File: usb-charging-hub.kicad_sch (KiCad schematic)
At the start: 3 parts

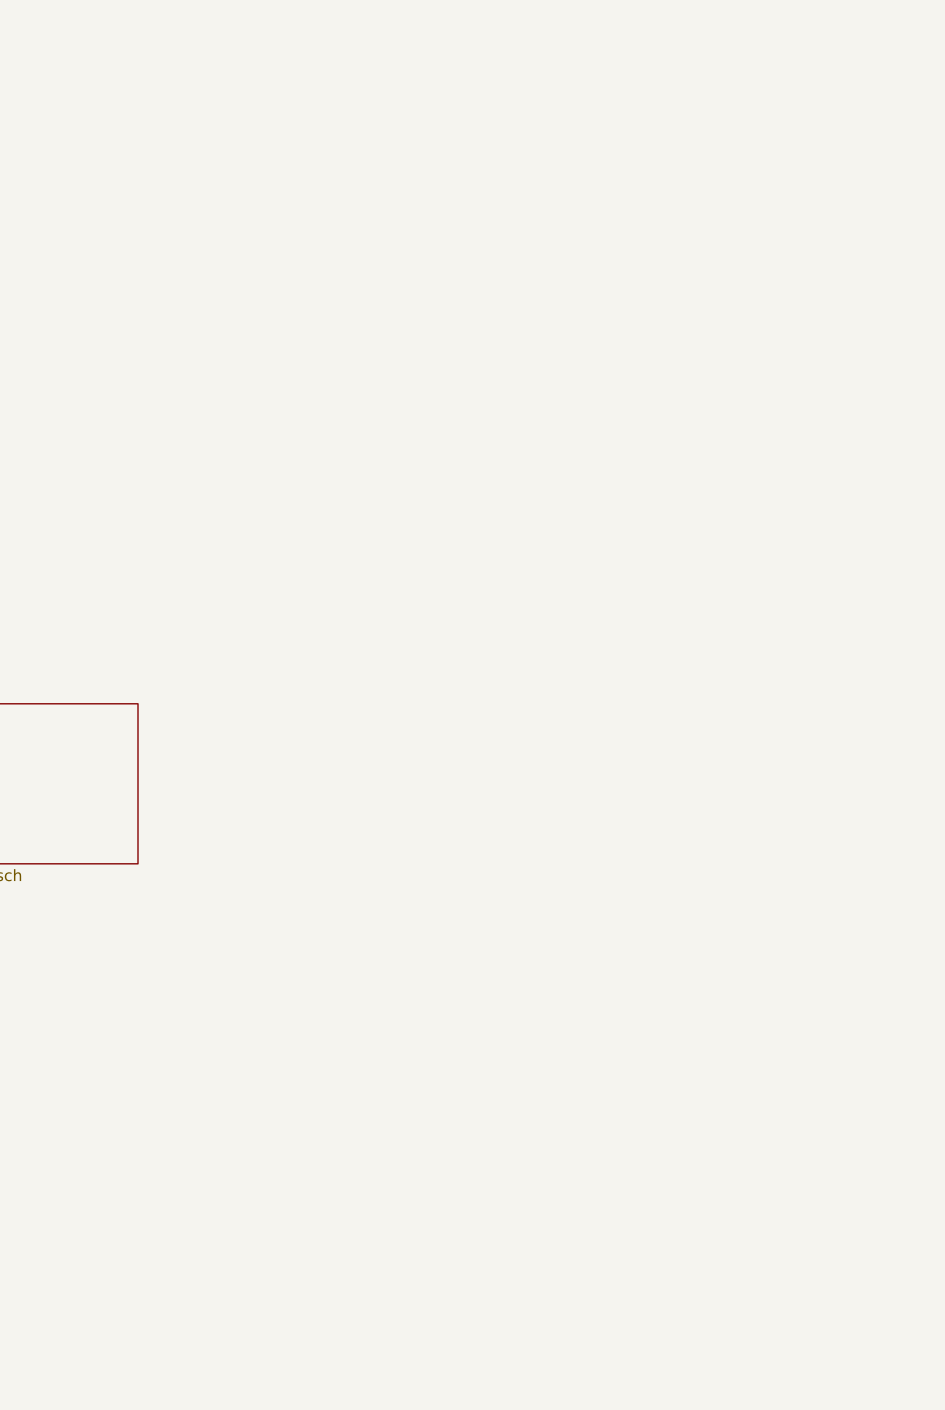
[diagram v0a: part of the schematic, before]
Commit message: fixed wrong wiring of 5V regulator for rp mcu + added all usb a ports
Signed-off-by: Toby Cm <toby@vsus.app>
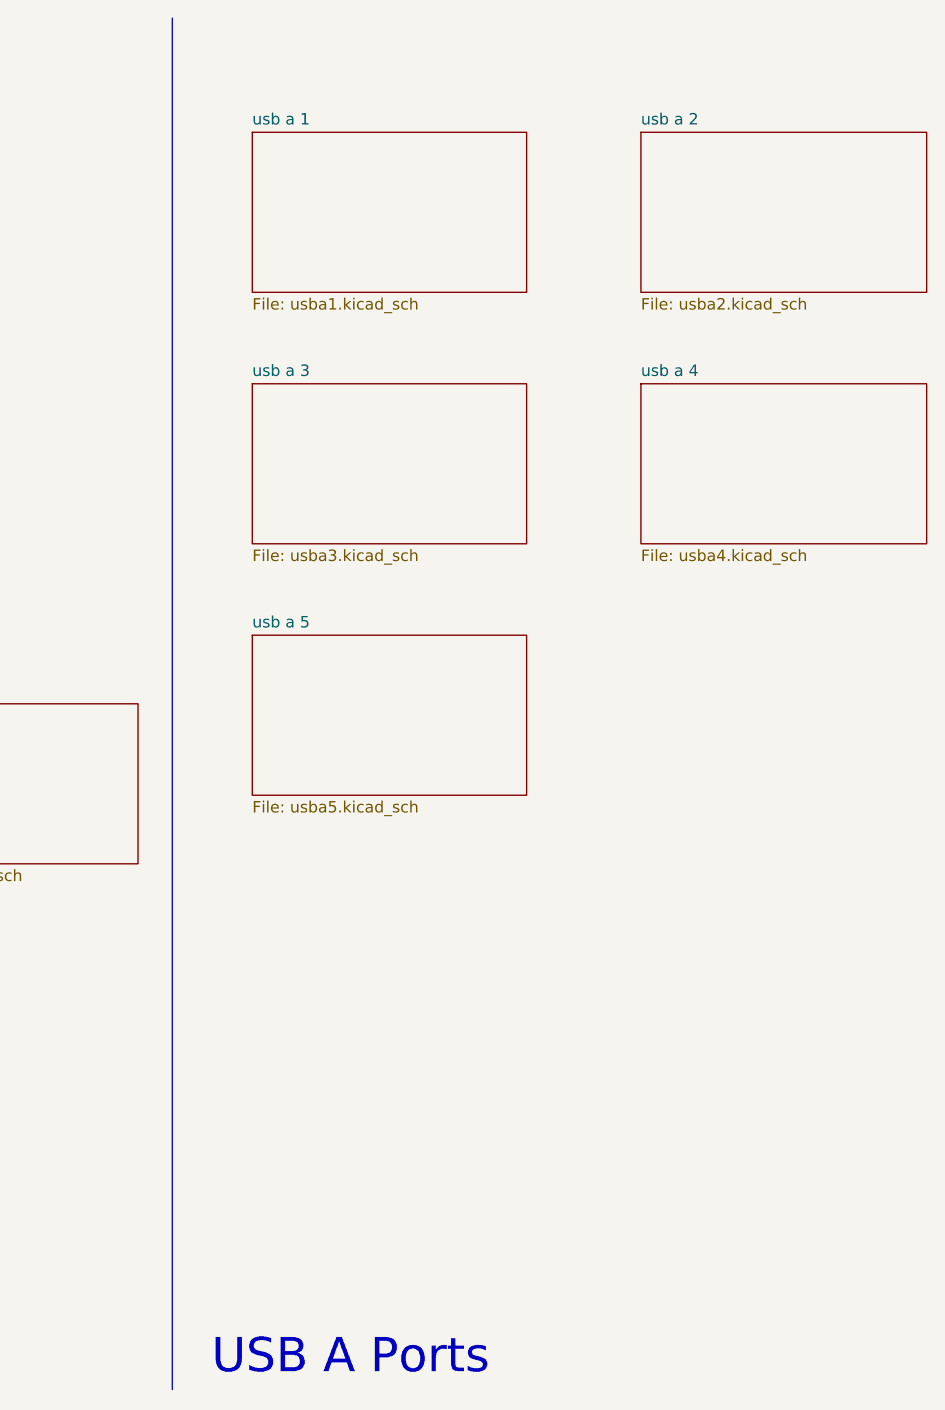
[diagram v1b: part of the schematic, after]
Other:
- added sheet usb a 1 (usba1.kicad_sch)
- added sheet usb a 2 (usba2.kicad_sch)
- added sheet usb a 3 (usba3.kicad_sch)
- added sheet usb a 4 (usba4.kicad_sch)
- added sheet usb a 5 (usba5.kicad_sch)
- note added: "USB A Ports"
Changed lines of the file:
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@@
 		(company "DaCloud")
+	)
+	(text "USB A Ports"
+		(exclude_from_sim no)
+		(at 211.582 161.544 0)
+		(effects
+			(font
+				(size 3.81 3.81)
+			)
+		)
 	)
 	(text "power led\n"
@@
 		)
 	)
+	(polyline
+		(pts
+			(xy 191.77 12.7) (xy 191.77 165.1)
+		)
+		(stroke
+			(width 0)
+			(type default)
+		)
+	)
 	(symbol
 		(lib_id "Jumper:SolderJumper_2_Bridged")
@@
 	)
 	(sheet
+		(at 243.84 25.4)
+		(size 31.75 17.78)
+		(exclude_from_sim no)
+		(in_bom yes)
+		(on_board yes)
+		(dnp no)
+		(fields_autoplaced yes)
+		(stroke
+			(width 0.1524)
+			(type solid)
+		)
+		(fill
+			(color 0 0 0 0.0000)
+		)
+		(property "Sheetname" "usb a 2"
+			(at 243.84 24.6884 0)
+			(effects
+				(font
+					(size 1.27 1.27)
+				)
+				(justify left bottom)
+			)
+		)
+		(property "Sheetfile" "usba2.kicad_sch"
+			(at 243.84 43.7646 0)
+			(effects
+				(font
+					(size 1.27 1.27)
+				)
+				(justify left top)
+			)
+		)
+		(instances
+			(project "usb-charging-hub"
+				(path "/04e54dfe-f06f-40ed-b860-573373578cb0"
+					(page "7")
+				)
+			)
+		)
+	)
+	(sheet
 		(at 22.86 88.9)
 		(size 30.48 17.78)
@@
 	)
 	(sheet
+		(at 200.66 81.28)
+		(size 30.48 17.78)
+		(exclude_from_sim no)
+		(in_bom yes)
+		(on_board yes)
+		(dnp no)
+		(fields_autoplaced yes)
+		(stroke
+			(width 0.1524)
+			(type solid)
+		)
+		(fill
+			(color 0 0 0 0.0000)
+		)
+		(property "Sheetname" "usb a 5"
+			(at 200.66 80.5684 0)
+			(effects
+				(font
+					(size 1.27 1.27)
+				)
+				(justify left bottom)
+			)
+		)
+		(property "Sheetfile" "usba5.kicad_sch"
+			(at 200.66 99.6446 0)
+			(effects
+				(font
+					(size 1.27 1.27)
+				)
+				(justify left top)
+			)
+		)
+		(instances
+			(project "usb-charging-hub"
+				(path "/04e54dfe-f06f-40ed-b860-573373578cb0"
+					(page "10")
+				)
+			)
+		)
+	)
+	(sheet
 		(at 66.04 88.9)
 		(size 31.75 17.78)
@@
 	)
 	(sheet
+		(at 200.66 25.4)
+		(size 30.48 17.78)
+		(exclude_from_sim no)
+		(in_bom yes)
+		(on_board yes)
+		(dnp no)
+		(fields_autoplaced yes)
+		(stroke
+			(width 0.1524)
+			(type solid)
+		)
+		(fill
+			(color 0 0 0 0.0000)
+		)
+		(property "Sheetname" "usb a 1"
+			(at 200.66 24.6884 0)
+			(effects
+				(font
+					(size 1.27 1.27)
+				)
+				(justify left bottom)
+			)
+		)
+		(property "Sheetfile" "usba1.kicad_sch"
+			(at 200.66 43.7646 0)
+			(effects
+				(font
+					(size 1.27 1.27)
+				)
+				(justify left top)
+			)
+		)
+		(instances
+			(project "usb-charging-hub"
+				(path "/04e54dfe-f06f-40ed-b860-573373578cb0"
+					(page "6")
+				)
+			)
+		)
+	)
+	(sheet
 		(at 109.22 88.9)
 		(size 33.02 17.78)
@@
 				)
 			)
+		)
+	)
+	(sheet
+		(at 243.84 53.34)
+		(size 31.75 17.78)
+		(exclude_from_sim no)
+		(in_bom yes)
+		(on_board yes)
+		(dnp no)
+		(fields_autoplaced yes)
+		(stroke
+			(width 0.1524)
+			(type solid)
+		)
+		(fill
+			(color 0 0 0 0.0000)
+		)
+		(property "Sheetname" "usb a 4"
+			(at 243.84 52.6284 0)
+			(effects
+				(font
+					(size 1.27 1.27)
+				)
+				(justify left bottom)
+			)
+		)
+		(property "Sheetfile" "usba4.kicad_sch"
+			(at 243.84 71.7046 0)
+			(effects
+				(font
+					(size 1.27 1.27)
+				)
+				(justify left top)
+			)
+		)
+		(instances
+			(project "usb-charging-hub"
+				(path "/04e54dfe-f06f-40ed-b860-573373578cb0"
+					(page "9")
+				)
+			)
+		)
+	)
+	(sheet
+		(at 200.66 53.34)
+		(size 30.48 17.78)
+		(exclude_from_sim no)
+		(in_bom yes)
+		(on_board yes)
+		(dnp no)
+		(fields_autoplaced yes)
+		(stroke
+			(width 0.1524)
+			(type solid)
+		)
+		(fill
+			(color 0 0 0 0.0000)
+		)
+		(property "Sheetname" "usb a 3"
+			(at 200.66 52.6284 0)
+			(effects
+				(font
+					(size 1.27 1.27)
+				)
+				(justify left bottom)
+			)
+		)
+		(property "Sheetfile" "usba3.kicad_sch"
+			(at 200.66 71.7046 0)
+			(effects
+				(font
+					(size 1.27 1.27)
+				)
+				(justify left top)
+			)
+		)
+		(instances
+			(project "usb-charging-hub"
+				(path "/04e54dfe-f06f-40ed-b860-573373578cb0"
+					(page "8")
+				)
+			)

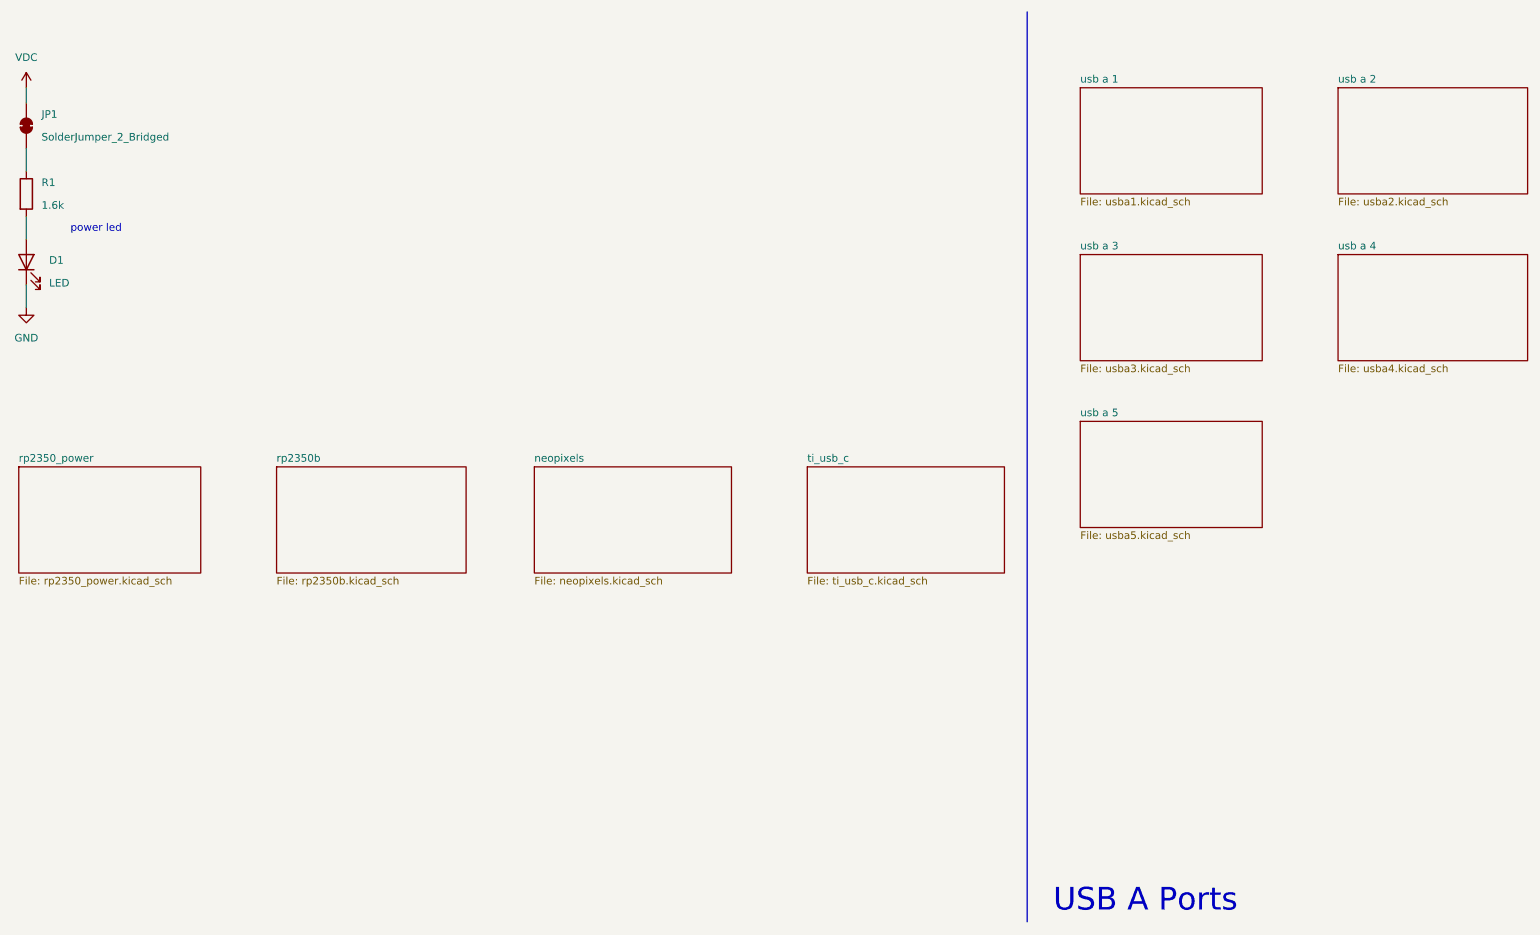
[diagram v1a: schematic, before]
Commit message: gave up on single board, gonna make small modules
Signed-off-by: Toby Cm <toby@vsus.app>
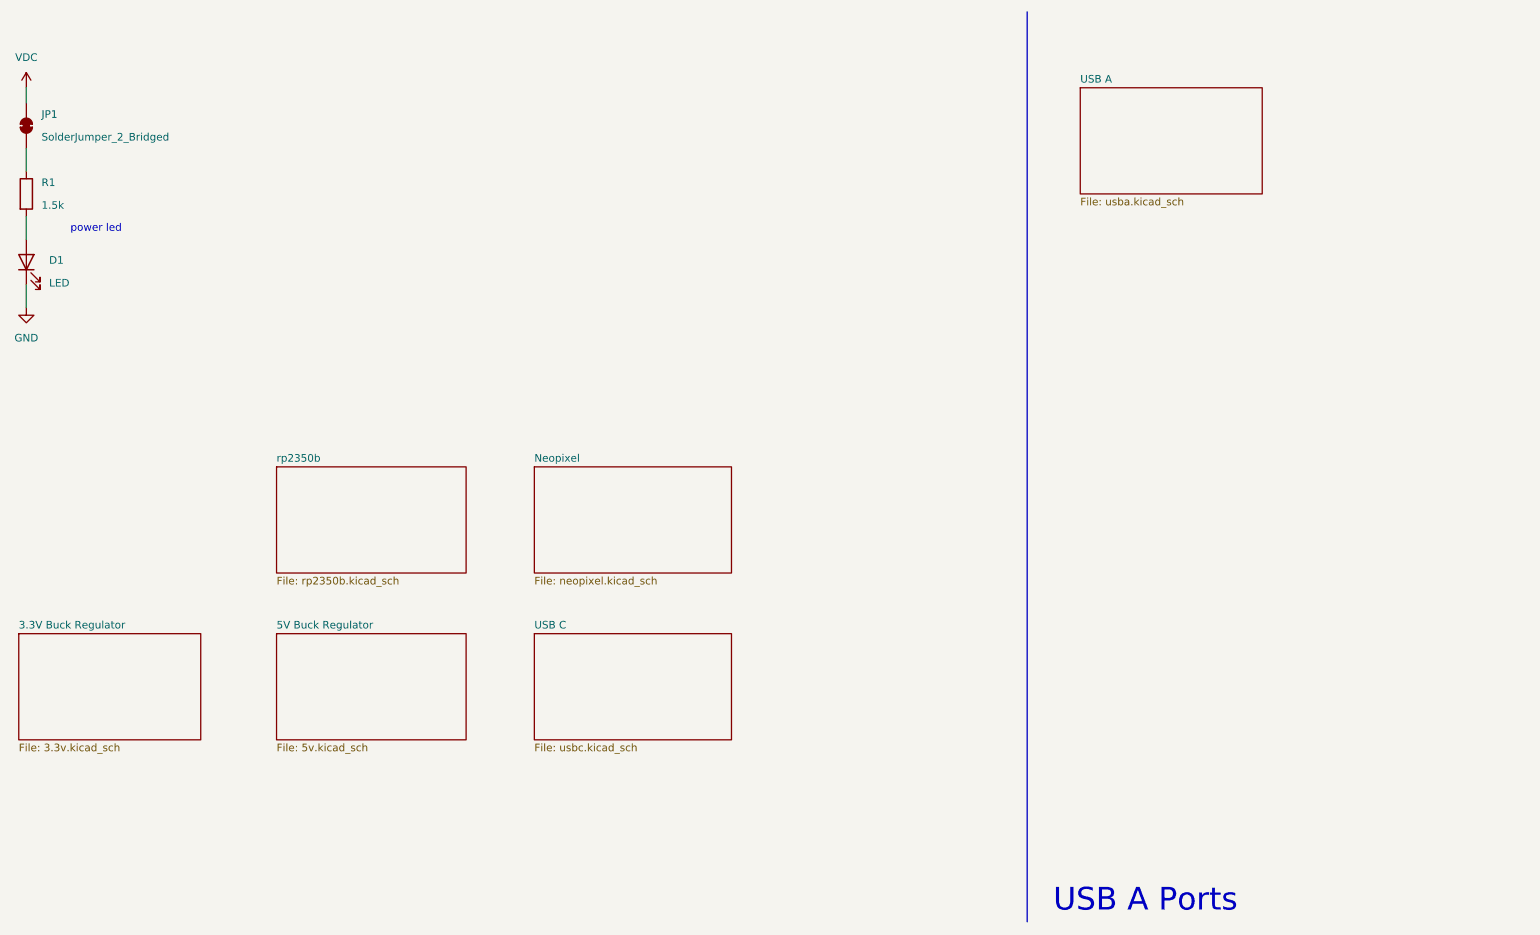
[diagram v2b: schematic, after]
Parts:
- D1: footprint (none) -> LED_SMD:LED_0603_1608Metric_Pad1.05x0.95mm_HandSolder
- JP1: footprint (none) -> Jumper:SolderJumper-2_P1.3mm_Bridged_Pad1.0x1.5mm
- R1: value 1.6k -> 1.5k; footprint (none) -> Resistor_SMD:R_1210_3225Metric_Pad1.30x2.65mm_HandSolder
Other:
- sheet neopixels renamed Neopixel
- sheet usb a 1 renamed USB A
- removed sheet rp2350_power
- removed sheet ti_usb_c
- removed sheet usb a 2
- removed sheet usb a 3
- removed sheet usb a 4
- removed sheet usb a 5
- added sheet 3.3V Buck Regulator (3.3v.kicad_sch)
- added sheet 5V Buck Regulator (5v.kicad_sch)
- added sheet USB C (usbc.kicad_sch)
- sheet Neopixel: file neopixels.kicad_sch -> neopixel.kicad_sch
- sheet USB A: file usba1.kicad_sch -> usba.kicad_sch
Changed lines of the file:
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@@
 			)
 		)
-		(property "Footprint" ""
+		(property "Footprint" "Jumper:SolderJumper-2_P1.3mm_Bridged_Pad1.0x1.5mm"
 			(at 24.13 31.75 0)
 			(effects
@@
 			)
 		)
-		(property "Value" "1.6k"
+		(property "Value" "1.5k"
 			(at 26.67 45.0849 0)
 			(effects
@@
 			)
 		)
-		(property "Footprint" ""
+		(property "Footprint" "Resistor_SMD:R_1210_3225Metric_Pad1.30x2.65mm_HandSolder"
 			(at 22.352 43.18 90)
 			(effects
@@
 			)
 		)
-		(property "Footprint" ""
+		(property "Footprint" "LED_SMD:LED_0603_1608Metric_Pad1.05x0.95mm_HandSolder"
 			(at 24.13 54.61 0)
 			(effects
@@
 	)
 	(sheet
-		(at 243.84 25.4)
+		(at 66.04 88.9)
 		(size 31.75 17.78)
 		(exclude_from_sim no)
@@
 			(color 0 0 0 0.0000)
 		)
-		(property "Sheetname" "usb a 2"
-			(at 243.84 24.6884 0)
+		(property "Sheetname" "rp2350b"
+			(at 66.04 88.1884 0)
 			(effects
 				(font
@@
 			)
 		)
-		(property "Sheetfile" "usba2.kicad_sch"
-			(at 243.84 43.7646 0)
+		(property "Sheetfile" "rp2350b.kicad_sch"
+			(at 66.04 107.2646 0)
 			(effects
 				(font
@@
 			(project "usb-charging-hub"
 				(path "/04e54dfe-f06f-40ed-b860-573373578cb0"
-					(page "7")
+					(page "3")
 				)
 			)
@@
 	)
 	(sheet
-		(at 22.86 88.9)
+		(at 200.66 25.4)
 		(size 30.48 17.78)
 		(exclude_from_sim no)
@@
 			(color 0 0 0 0.0000)
 		)
-		(property "Sheetname" "rp2350_power"
-			(at 22.86 88.1884 0)
+		(property "Sheetname" "USB A"
+			(at 200.66 24.6884 0)
 			(effects
 				(font
@@
 			)
 		)
-		(property "Sheetfile" "rp2350_power.kicad_sch"
-			(at 22.86 107.2646 0)
+		(property "Sheetfile" "usba.kicad_sch"
+			(at 200.66 43.7646 0)
 			(effects
 				(font
@@
 			(project "usb-charging-hub"
 				(path "/04e54dfe-f06f-40ed-b860-573373578cb0"
-					(page "2")
+					(page "6")
 				)
 			)
@@
 	)
 	(sheet
-		(at 154.94 88.9)
+		(at 109.22 116.84)
 		(size 33.02 17.78)
 		(exclude_from_sim no)
@@
 			(color 0 0 0 0.0000)
 		)
-		(property "Sheetname" "ti_usb_c"
-			(at 154.94 88.1884 0)
+		(property "Sheetname" "USB C"
+			(at 109.22 116.1284 0)
 			(effects
 				(font
@@
 			)
 		)
-		(property "Sheetfile" "ti_usb_c.kicad_sch"
-			(at 154.94 107.2646 0)
+		(property "Sheetfile" "usbc.kicad_sch"
+			(at 109.22 135.2046 0)
 			(effects
 				(font
@@
 			(project "usb-charging-hub"
 				(path "/04e54dfe-f06f-40ed-b860-573373578cb0"
-					(page "5")
+					(page "9")
 				)
 			)
@@
 	)
 	(sheet
-		(at 200.66 81.28)
-		(size 30.48 17.78)
+		(at 109.22 88.9)
+		(size 33.02 17.78)
 		(exclude_from_sim no)
 		(in_bom yes)
@@
 			(color 0 0 0 0.0000)
 		)
-		(property "Sheetname" "usb a 5"
-			(at 200.66 80.5684 0)
+		(property "Sheetname" "Neopixel"
+			(at 109.22 88.1884 0)
 			(effects
 				(font
@@
 			)
 		)
-		(property "Sheetfile" "usba5.kicad_sch"
-			(at 200.66 99.6446 0)
+		(property "Sheetfile" "neopixel.kicad_sch"
+			(at 109.22 107.2646 0)
 			(effects
 				(font
@@
 			(project "usb-charging-hub"
 				(path "/04e54dfe-f06f-40ed-b860-573373578cb0"
-					(page "10")
+					(page "4")
 				)
 			)
@@
 	)
 	(sheet
-		(at 66.04 88.9)
+		(at 66.04 116.84)
 		(size 31.75 17.78)
 		(exclude_from_sim no)
@@
 			(color 0 0 0 0.0000)
 		)
-		(property "Sheetname" "rp2350b"
-			(at 66.04 88.1884 0)
+		(property "Sheetname" "5V Buck Regulator"
+			(at 66.04 116.1284 0)
 			(effects
 				(font
@@
 			)
 		)
-		(property "Sheetfile" "rp2350b.kicad_sch"
-			(at 66.04 107.2646 0)
+		(property "Sheetfile" "5v.kicad_sch"
+			(at 66.04 135.2046 0)
 			(effects
 				(font
@@
 			(project "usb-charging-hub"
 				(path "/04e54dfe-f06f-40ed-b860-573373578cb0"
-					(page "3")
+					(page "8")
 				)
 			)
@@
 	)
 	(sheet
-		(at 200.66 25.4)
+		(at 22.86 116.84)
 		(size 30.48 17.78)
 		(exclude_from_sim no)
@@
 			(color 0 0 0 0.0000)
 		)
-		(property "Sheetname" "usb a 1"
-			(at 200.66 24.6884 0)
+		(property "Sheetname" "3.3V Buck Regulator"
+			(at 22.86 116.1284 0)
 			(effects
 				(font
@@
 			)
 		)
-		(property "Sheetfile" "usba1.kicad_sch"
-			(at 200.66 43.7646 0)
+		(property "Sheetfile" "3.3v.kicad_sch"
+			(at 22.86 135.2046 0)
 			(effects
 				(font
@@
 			(project "usb-charging-hub"
 				(path "/04e54dfe-f06f-40ed-b860-573373578cb0"
-					(page "6")
-				)
-			)
-		)
-	)
-	(sheet
-		(at 109.22 88.9)
-		(size 33.02 17.78)
-		(exclude_from_sim no)
-		(in_bom yes)
-		(on_board yes)
-		(dnp no)
-		(fields_autoplaced yes)
-		(stroke
-			(width 0.1524)
-			(type solid)
-		)
-		(fill
-			(color 0 0 0 0.0000)
-		)
-		(property "Sheetname" "neopixels"
-			(at 109.22 88.1884 0)
-			(effects
-				(font
-					(size 1.27 1.27)
-				)
-				(justify left bottom)
-			)
-		)
-		(property "Sheetfile" "neopixels.kicad_sch"
-			(at 109.22 107.2646 0)
-			(effects
-				(font
-					(size 1.27 1.27)
-				)
-				(justify left top)
-			)
-		)
-		(instances
-			(project "usb-charging-hub"
-				(path "/04e54dfe-f06f-40ed-b860-573373578cb0"
-					(page "4")
-				)
-			)
-		)
-	)
-	(sheet
-		(at 243.84 53.34)
-		(size 31.75 17.78)
-		(exclude_from_sim no)
-		(in_bom yes)
-		(on_board yes)
-		(dnp no)
-		(fields_autoplaced yes)
-		(stroke
-			(width 0.1524)
-			(type solid)
-		)
-		(fill
-			(color 0 0 0 0.0000)
-		)
-		(property "Sheetname" "usb a 4"
-			(at 243.84 52.6284 0)
-			(effects
-				(font
-					(size 1.27 1.27)
-				)
-				(justify left bottom)
-			)
-		)
-		(property "Sheetfile" "usba4.kicad_sch"
-			(at 243.84 71.7046 0)
-			(effects
-				(font
-					(size 1.27 1.27)
-				)
-				(justify left top)
-			)
-		)
-		(instances
-			(project "usb-charging-hub"
-				(path "/04e54dfe-f06f-40ed-b860-573373578cb0"
-					(page "9")
-				)
-			)
-		)
-	)
-	(sheet
-		(at 200.66 53.34)
-		(size 30.48 17.78)
-		(exclude_from_sim no)
-		(in_bom yes)
-		(on_board yes)
-		(dnp no)
-		(fields_autoplaced yes)
-		(stroke
-			(width 0.1524)
-			(type solid)
-		)
-		(fill
-			(color 0 0 0 0.0000)
-		)
-		(property "Sheetname" "usb a 3"
-			(at 200.66 52.6284 0)
-			(effects
-				(font
-					(size 1.27 1.27)
-				)
-				(justify left bottom)
-			)
-		)
-		(property "Sheetfile" "usba3.kicad_sch"
-			(at 200.66 71.7046 0)
-			(effects
-				(font
-					(size 1.27 1.27)
-				)
-				(justify left top)
-			)
-		)
-		(instances
-			(project "usb-charging-hub"
-				(path "/04e54dfe-f06f-40ed-b860-573373578cb0"
-					(page "8")
-				)
-			)
+					(page "7")
+				)
+			)
